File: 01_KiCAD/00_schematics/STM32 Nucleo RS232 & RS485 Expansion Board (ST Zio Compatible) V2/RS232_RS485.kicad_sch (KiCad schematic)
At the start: 51 parts, among them J1 HD-A(Y), J2 HD-B(Z), J3 TERM_RX (A/B), J4 TERM_TX (Y/Z), J5 1190299, J6 CONN D-SUB PLUG 9POS TH, J7 TCVR_PWR, U3 THVD4431RHAR

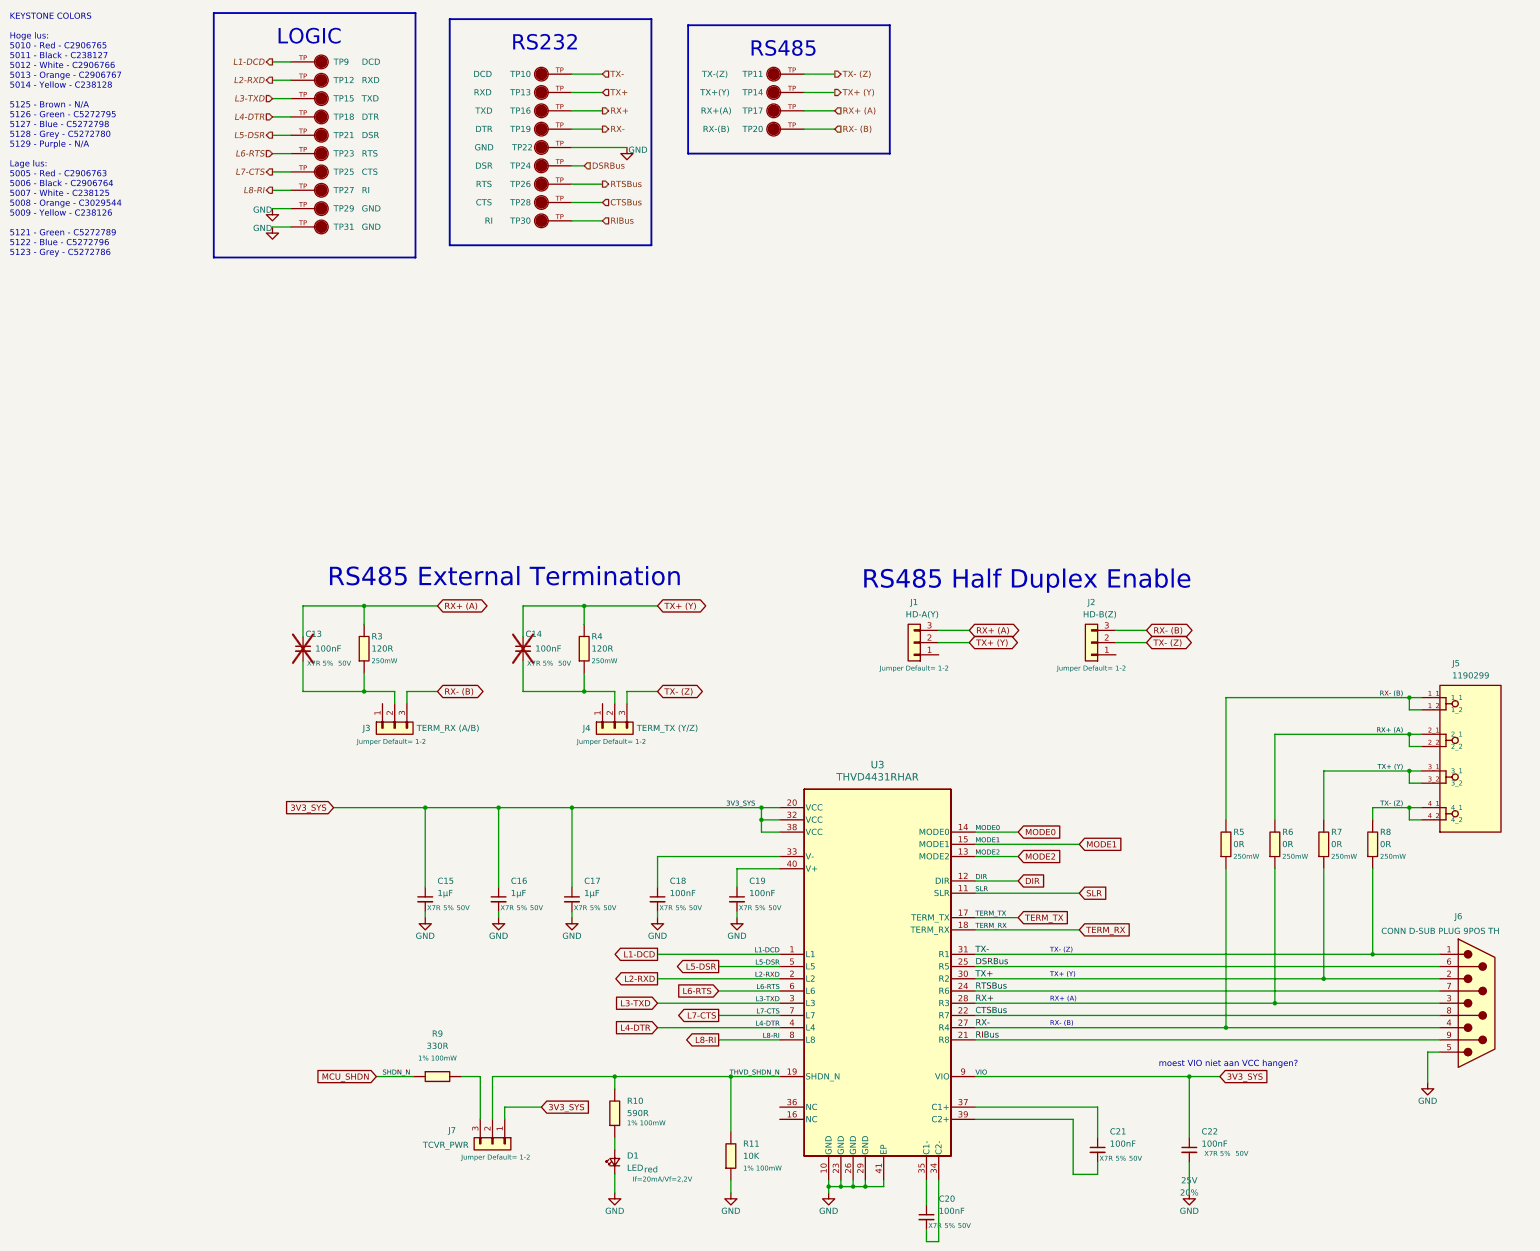
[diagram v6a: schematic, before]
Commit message: Updating routing
Update routing tracks and placing and re-ordering components on the board.
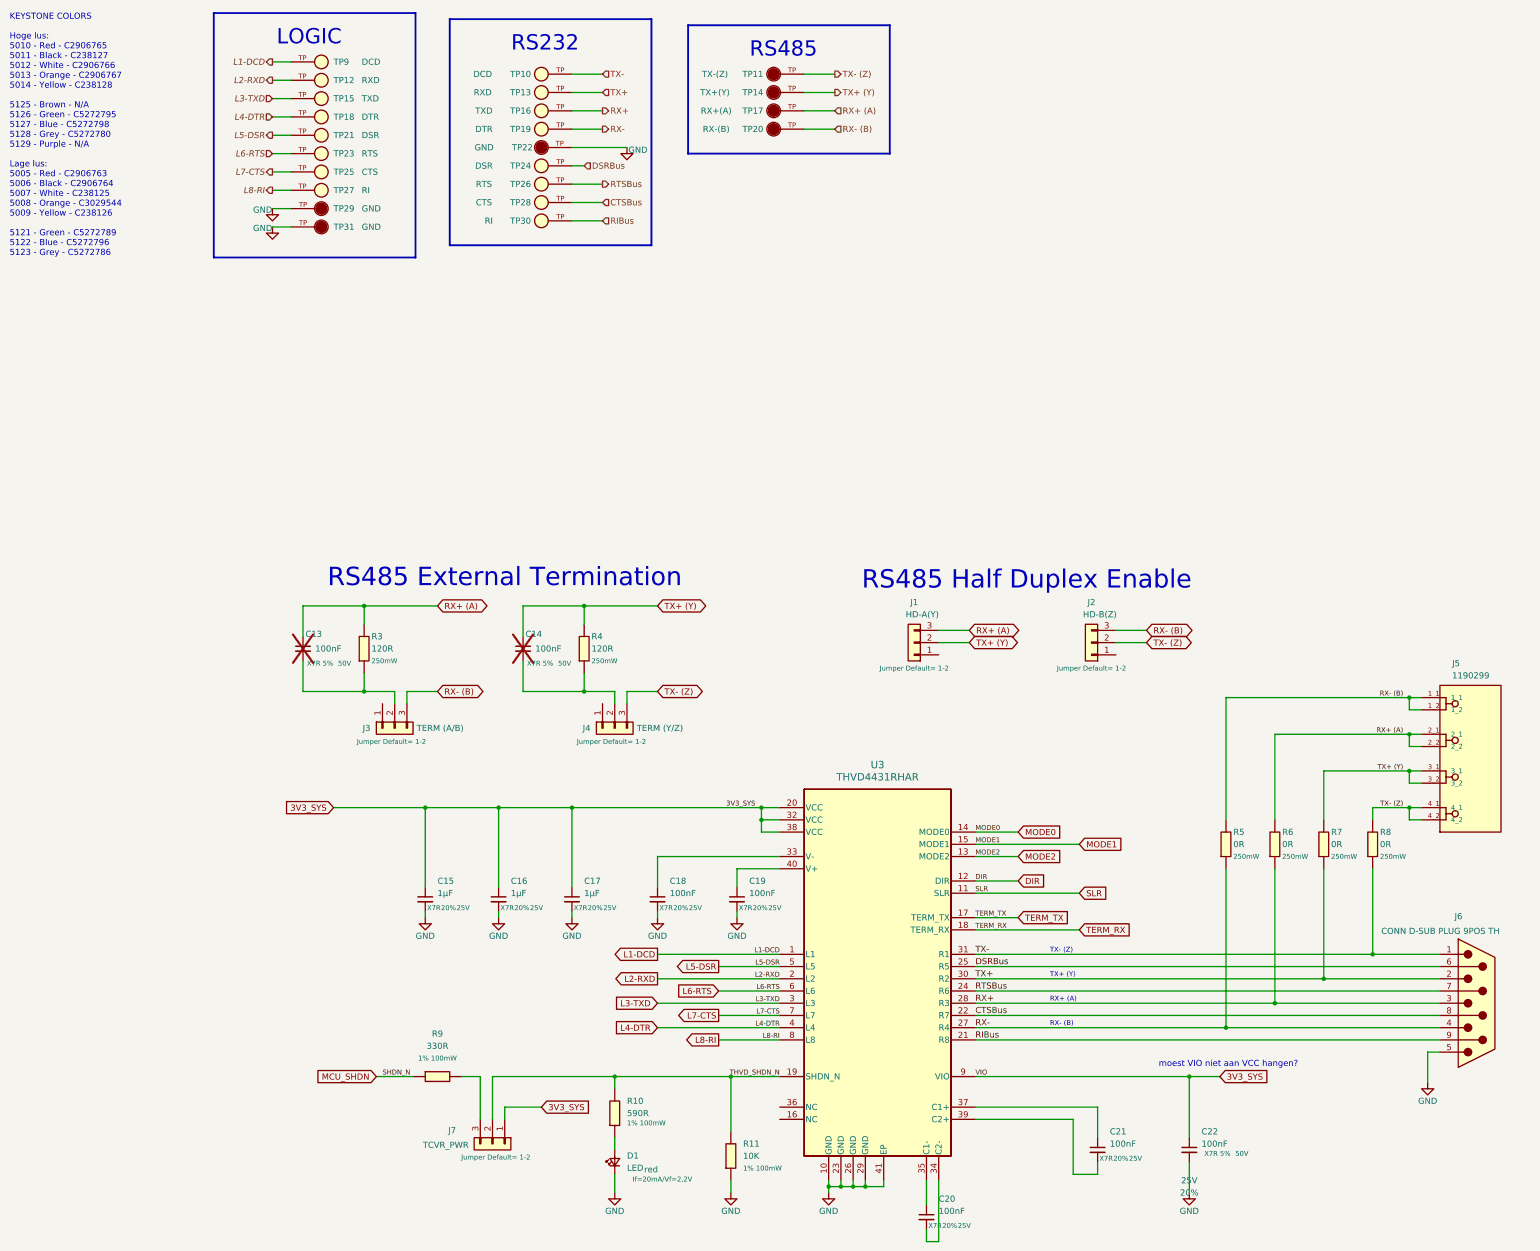
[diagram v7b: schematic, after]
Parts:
- C15, C16, C17: Tolerance 5% -> 20%; Voltage 50V -> 25V
- C18, C19, C20, C21: PROD_ID (none) -> CAP-00810; Tolerance 5% -> 20%; Voltage 50V -> 25V
- J3: value TERM_RX (A/B) -> TERM (A/B)
- J4: value TERM_TX (Y/Z) -> TERM (Y/Z)
- TP10, TP13: footprint 5009_Yellow:KEYSTONE_5009 -> 5122_Blue:KEYSTONE_5122; symbol 5009_Yellow:5009 -> 5122_Blue:5122; Check_prices https://www.snapeda.com/parts/5009/Keystone/view-part/?ref=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 -> https://www.snapeda.com/parts/5122/Keystone/view-part/?ref=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; Description_1 Test Point Compact THM H .350 Nylon46 Insulated Yellow Phos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 -> Blue PC Test Point, Compact Phosphor Bronze Silver Plating 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; MF Keystone Electronics Corp. -> Keystone Electronics; MP 5009 -> 5122; Package NON STANDARD-1 Keystone -> None; Purchase-URL (none) -> https://www.snapeda.com/api/url_track_click_mouser/?unipart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; SnapEDA_Link https://www.snapeda.com/parts/5009/Keystone/view-part/?ref=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 -> https://www.snapeda.com/parts/5122/Keystone/view-part/?ref=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
- TP12, TP15, TP18, TP21, TP23, TP25, TP27, TP9: footprint 5009_Yellow:KEYSTONE_5009 -> 5121_Green:KEYSTONE_5121; symbol 5009_Yellow:5009 -> 5121_Green:5121; Check_prices https://www.snapeda.com/parts/5009/Keystone/view-part/?ref=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 -> https://www.snapeda.com/parts/5121/Keystone/view-part/?ref=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; Description_1 Test Point Compact THM H .350 Nylon46 Insulated Yellow Phos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 -> Compact THM Test Point -Green; MF Keystone Electronics Corp. -> Keystone Electronics; MP 5009 -> 5121; Package NON STANDARD-1 Keystone -> None; Purchase-URL (none) -> https://www.snapeda.com/api/url_track_click_mouser/?unipart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; SnapEDA_Link https://www.snapeda.com/parts/5009/Keystone/view-part/?ref=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 -> https://www.snapeda.com/parts/5121/Keystone/view-part/?ref=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
- TP16, TP19, TP24, TP26, TP28, TP30: footprint 5008_Orange:KEYSTONE_5008 -> 5122_Blue:KEYSTONE_5122; symbol 5008_Orange:5008 -> 5122_Blue:5122; Check_prices https://www.snapeda.com/parts/5008/Keystone/view-part/?ref=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 -> https://www.snapeda.com/parts/5122/Keystone/view-part/?ref=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; Description_1 Compact THM Test Point -Orange -> Blue PC Test Point, Compact Phosphor Bronze Silver Plating 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; MP 5008 -> 5122; Package NON STANDARD-1 Keystone -> None; Purchase-URL (none) -> https://www.snapeda.com/api/url_track_click_mouser/?unipart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; SnapEDA_Link https://www.snapeda.com/parts/5008/Keystone/view-part/?ref=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 -> https://www.snapeda.com/parts/5122/Keystone/view-part/?ref=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

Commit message: Small changes to schematics & PCB work
Made some minor adjustments to the schematics, updated the PCB accordingly.
Placed all the components on the board and did some of the routing.
Updated the 3D models of all the components.
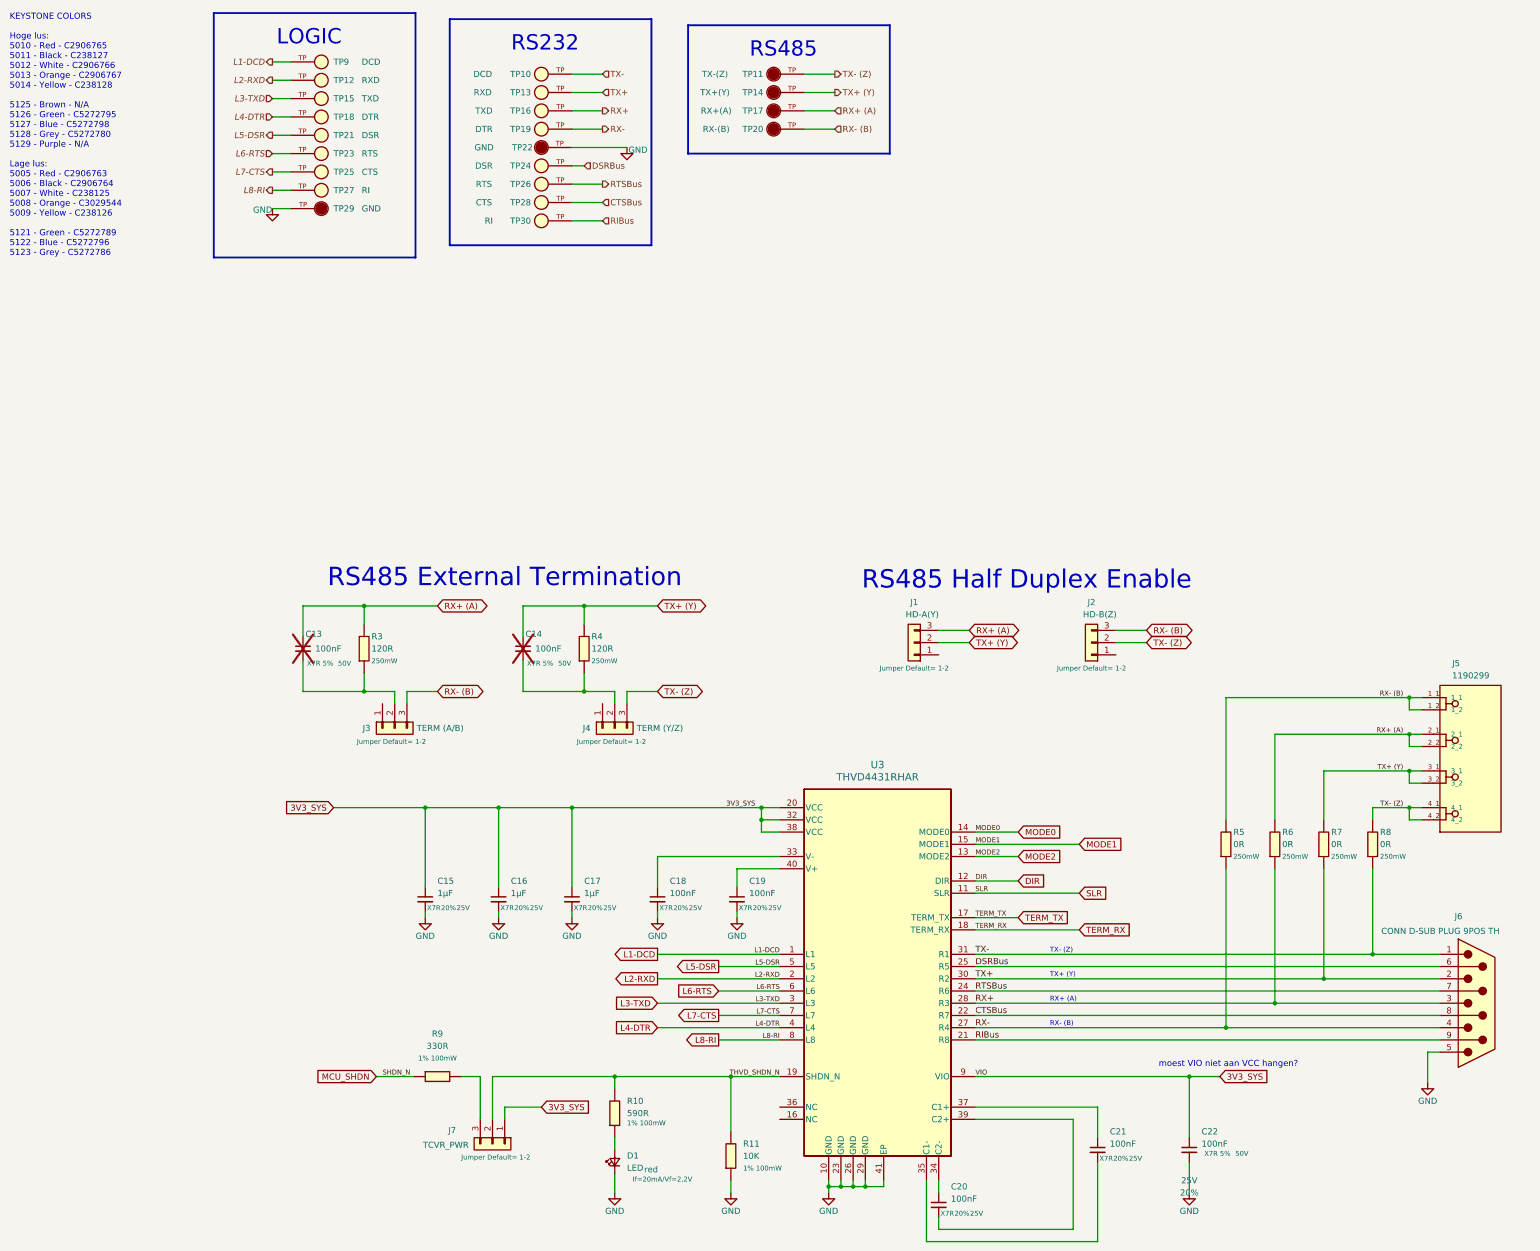
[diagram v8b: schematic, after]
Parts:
- removed TP31: GND, 5006_Black:KEYSTONE_5006, symbol 5006_Black:5006
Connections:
- net at U3.34 (C2-): now also C20.1; no longer C20.2
- net at U3.35 (C1-): now also C21.2; no longer C20.1
- net at U3.39 (C2+): now also C20.2; no longer C21.2
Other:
- moved on the sheet: C20
